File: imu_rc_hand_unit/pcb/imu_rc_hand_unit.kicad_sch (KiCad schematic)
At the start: 80 parts, among them J1 USB_C_Receptacle_USB2.0_16P, J2 JST SH1.0, Q1 IRLML6344TRPBF, Q2 IRLML6344TRPBF, Q3 DMP3160L-7, Q4 IRLML6344TRPBF, Q5 DMP3160L-7, Q6 BSS138, Q7 BC817-25, Q8 BC817-25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

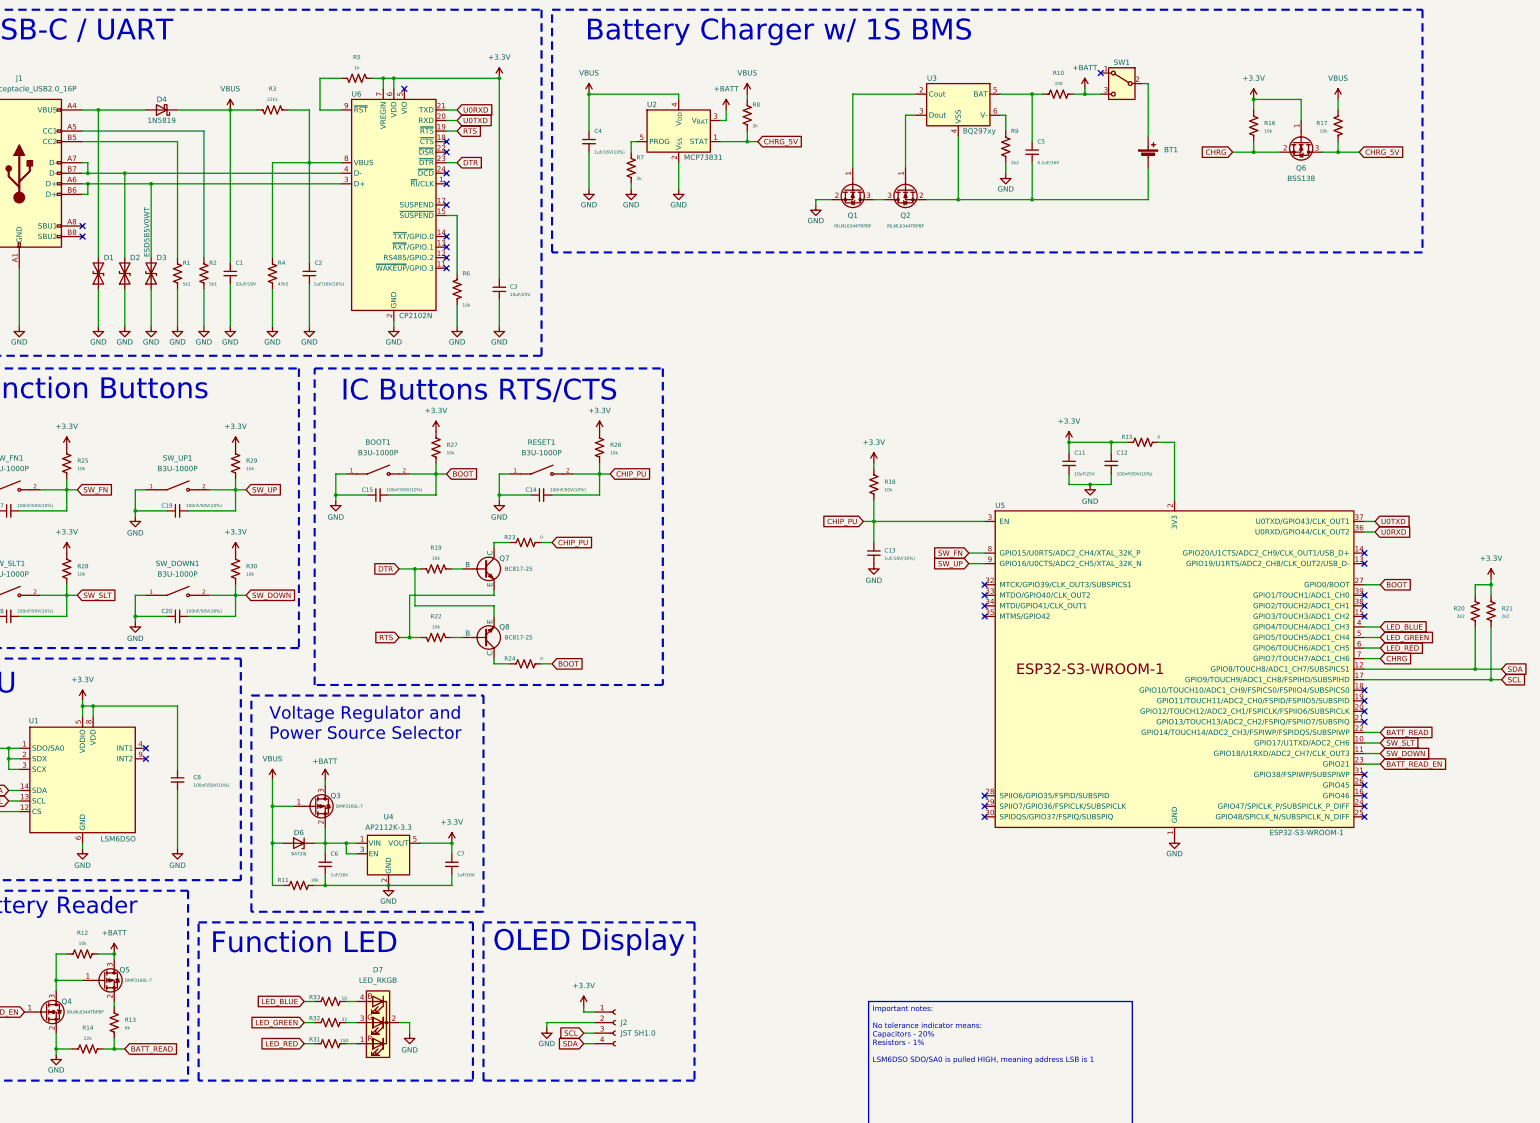
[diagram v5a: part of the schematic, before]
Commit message: commit #32
costs table 4
first revision of imu rc car pcb
imu rc encoders final version v1.0.0 (ordered)
imu rc prox sensors final version v1.0.0 (ordered)
minor resistors tolerance changes in hand unit
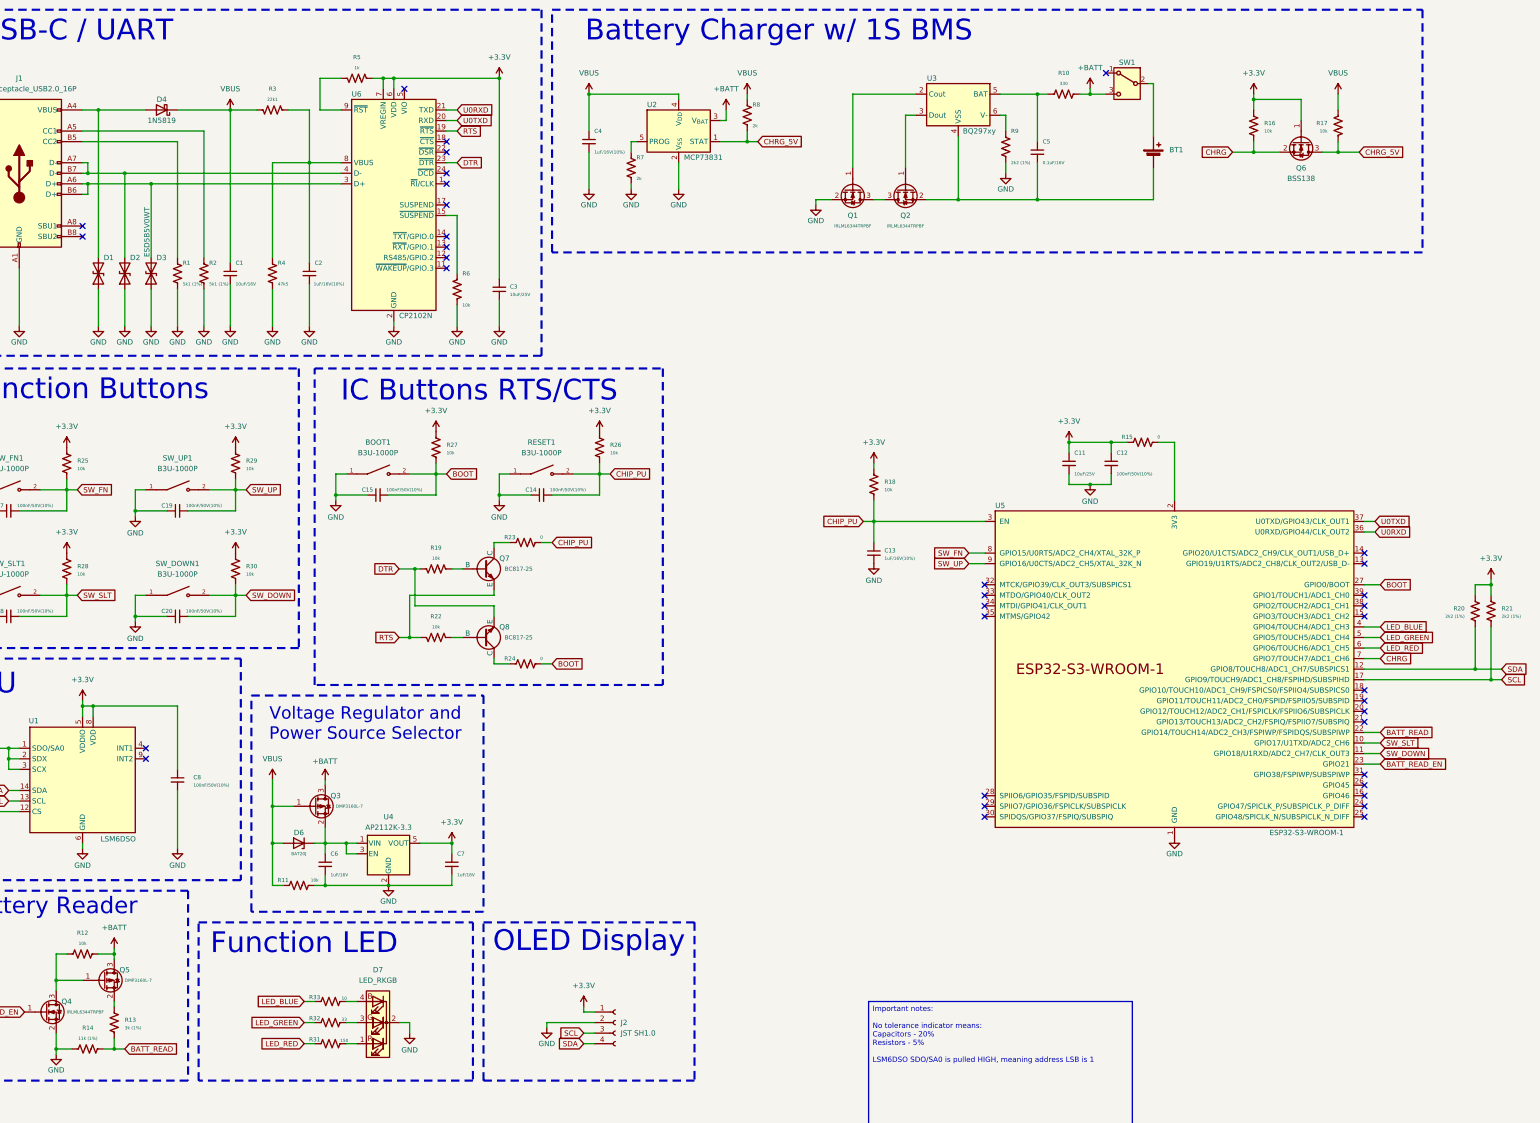
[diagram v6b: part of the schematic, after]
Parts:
- R1, R2: value 5k1 -> 5k1 (1%)
- R13: value 6k -> 3k (1%)
- R14: value 22k -> 11k (1%)
- R20, R21, R9: value 2k2 -> 2k2 (1%)
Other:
- moved on the sheet: BT1, C5, R10, SW1

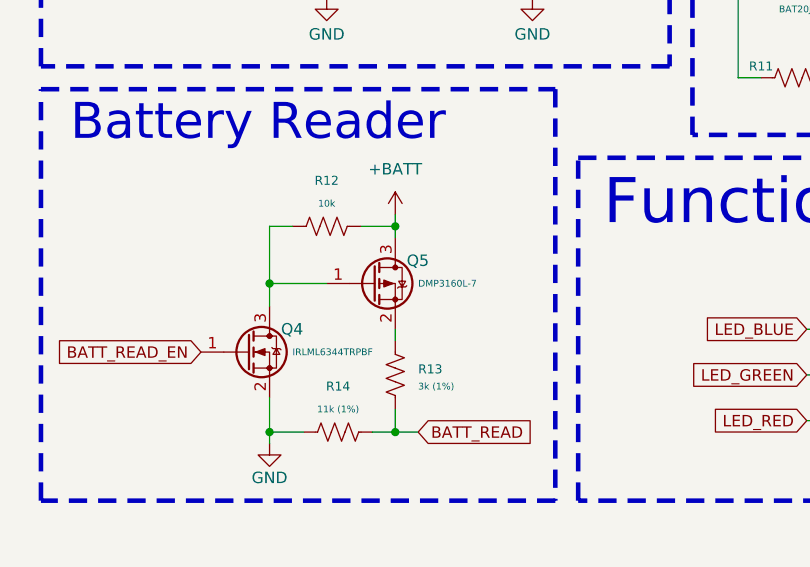
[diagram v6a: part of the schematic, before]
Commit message: commit #34
pcb hand unit v1.1.0:
chaged RGB led footprint to better fit
switch drain with source in Q5 MOSFET (battery reader)

pcb car v1.1.0:
removed power planes, added traces only
switch drain with source in Q1 MOSFET (battery reader)
changed LDO position

code:
changed esp32 devkit to esp32s3 devkit
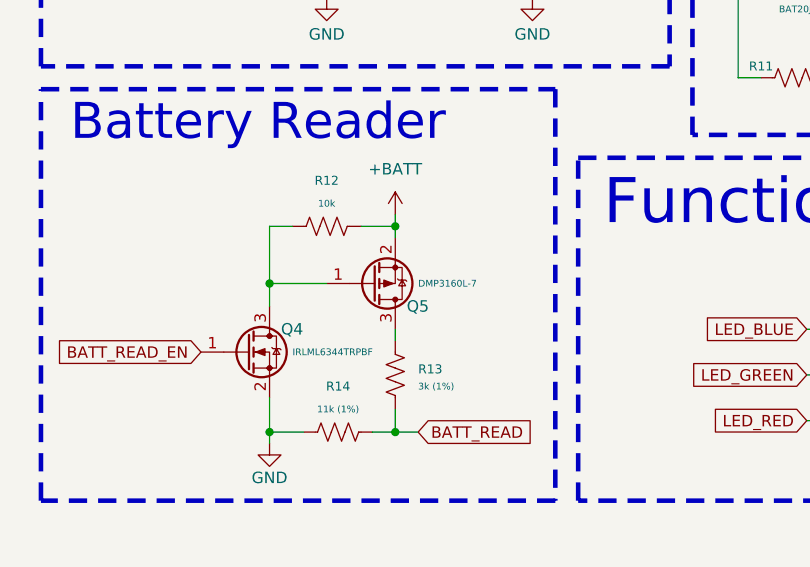
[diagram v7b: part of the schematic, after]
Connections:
- net +BATT: now also Q5.2 (S); no longer Q5.3 (D)
- net at R13.1: now also Q5.3 (D); no longer Q5.2 (S)
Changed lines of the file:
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@@
 		(lib_id "Transistor_FET:AO3401A")
 		(at 50.8 247.65 0)
+		(mirror x)
 		(unit 1)
 		(exclude_from_sim no)
@@
 		(dnp no)
 		(property "Reference" "Q5"
-			(at 54.61 245.11 0)
+			(at 54.61 250.19 0)
 			(effects
 				(font
@@
 		)
 		(property "Footprint" "Package_TO_SOT_SMD:SOT-23"
-			(at 55.88 249.555 0)
+			(at 55.88 245.745 0)
 			(effects
 				(font
@@
 		)
 		(property "Datasheet" "http://www.aosmd.com/pdfs/datasheet/AO3401A.pdf"
-			(at 55.88 251.46 0)
+			(at 55.88 243.84 0)
 			(effects
 				(font
